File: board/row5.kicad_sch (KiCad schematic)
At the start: 0 parts

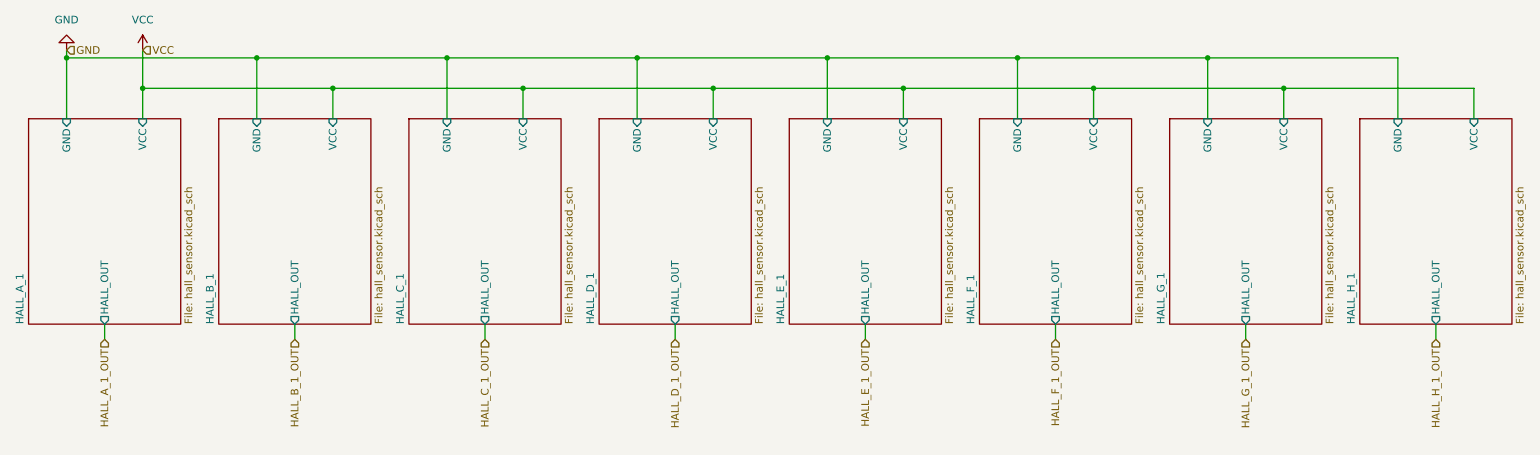
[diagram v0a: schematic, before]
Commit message: Connected all rows to MCPs
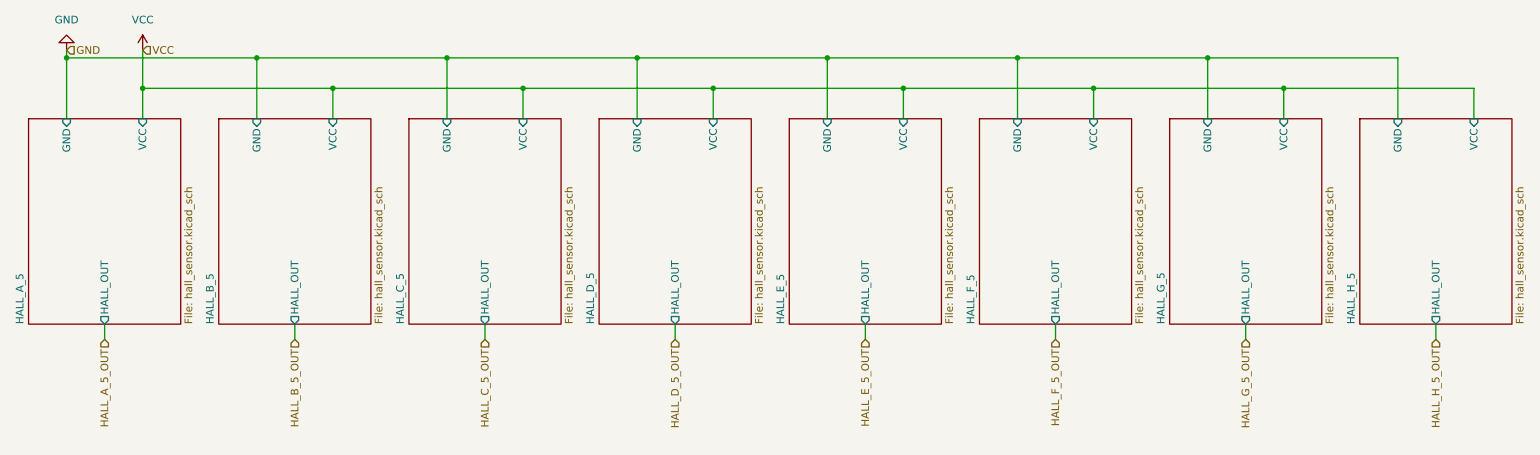
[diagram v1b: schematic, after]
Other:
- removed sheet HALL_A_1
- removed sheet HALL_B_1
- removed sheet HALL_C_1
- removed sheet HALL_D_1
- removed sheet HALL_E_1
- removed sheet HALL_F_1
- removed sheet HALL_G_1
- removed sheet HALL_H_1
- added sheet HALL_A_5 (hall_sensor.kicad_sch)
- added sheet HALL_B_5 (hall_sensor.kicad_sch)
- added sheet HALL_C_5 (hall_sensor.kicad_sch)
- added sheet HALL_D_5 (hall_sensor.kicad_sch)
- added sheet HALL_E_5 (hall_sensor.kicad_sch)
- added sheet HALL_F_5 (hall_sensor.kicad_sch)
- added sheet HALL_G_5 (hall_sensor.kicad_sch)
- added sheet HALL_H_5 (hall_sensor.kicad_sch)
